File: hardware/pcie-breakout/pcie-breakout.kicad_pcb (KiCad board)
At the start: 4 copper layers, 35 x 20.3 mm, 2 parts, among them J1 Bus_PCI_Express_x1, J2 Conn_01x10

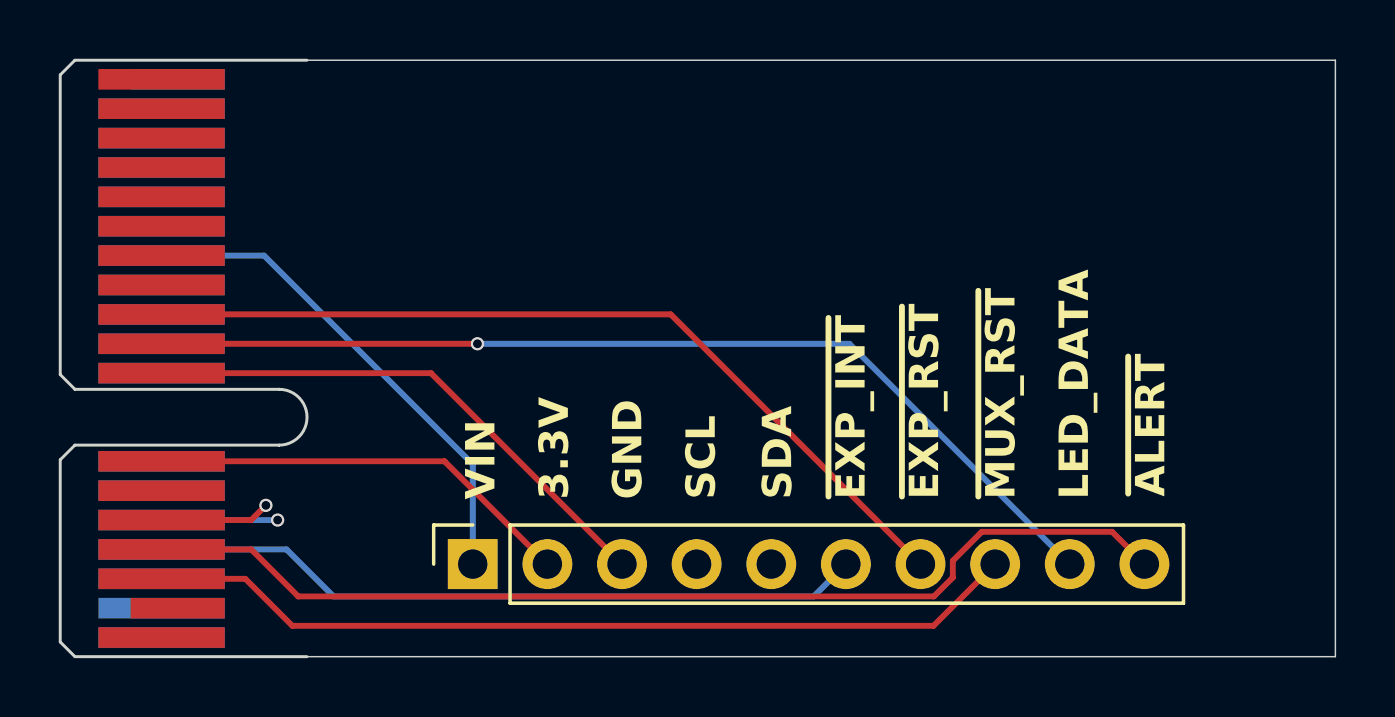
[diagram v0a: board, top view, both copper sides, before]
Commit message: chore(pcie-breakout): update 3.3v in to 5v
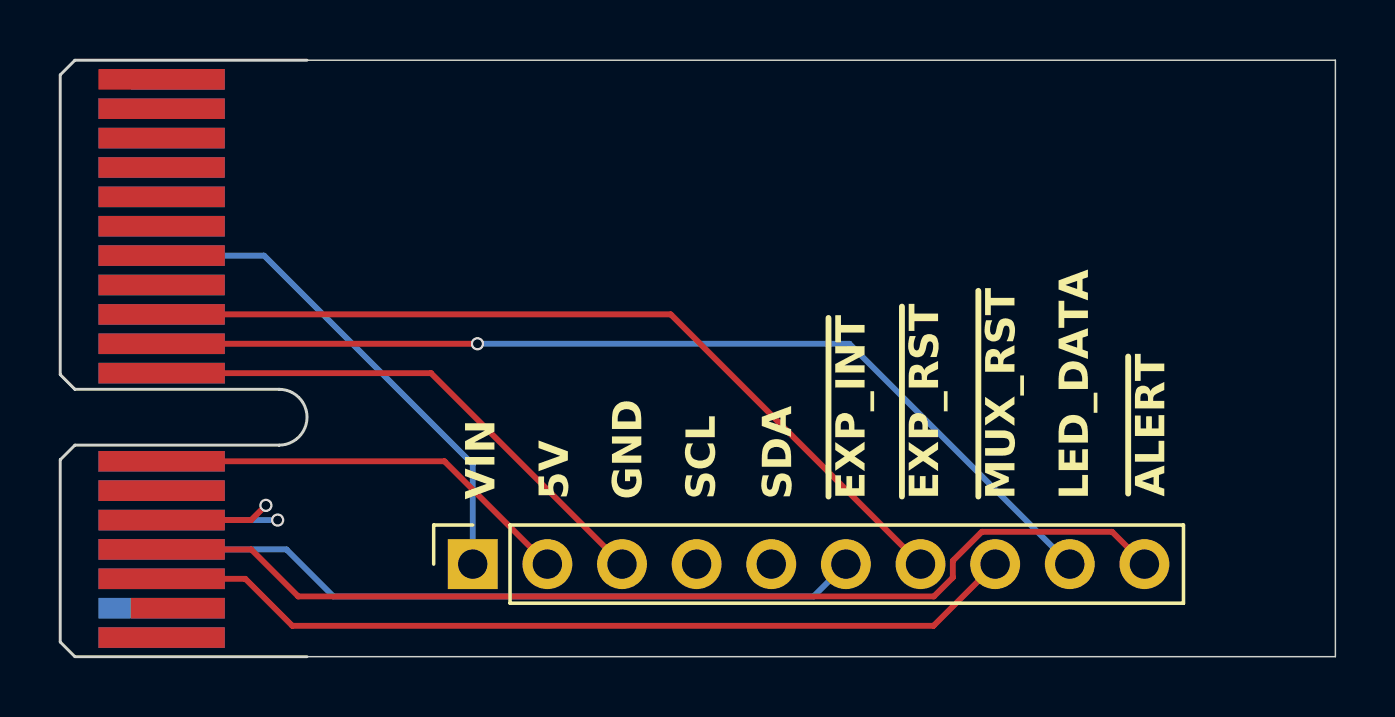
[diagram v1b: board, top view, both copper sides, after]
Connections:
- net +3.3V renamed +5V
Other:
- board text added: "5V"
- board text removed: "3.3V"
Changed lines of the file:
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@@
 		(capping no)
 		(filling no)
-		(zone_defaults)
 		(pcbplotparams
 			(layerselection 0x00000000_00000000_55555555_5755f5ff)
@@
 			)
 		)
-		(attr exclude_from_bom)
+		(attr dnp)
 		(duplicate_pad_numbers_are_jumpers no)
 		(fp_line
@@
 			(size 0.7 4.3)
 			(layers "B.Cu" "B.Mask")
-			(net "+3.3V")
-			(pinfunction "+3.3V_A12")
+			(net "+5V")
+			(pinfunction "+5V_A12")
 			(pintype "power_in")
 		)
@@
 			(size 0.7 4.3)
 			(layers "F.Cu" "F.Mask")
-			(net "+3.3V")
-			(pinfunction "+3.3V_B12")
+			(net "+5V")
+			(pinfunction "+5V_B12")
 			(pintype "passive")
 		)
@@
 			)
 		)
-		(property "Description" ""
+		(property "Description" "Generic connector, single row, 01x10, script generated (kicad-library-utils/schlib/autogen/connector/)"
 			(at 0 0 90)
 			(layer "F.Fab")
@@
 			(layers "*.Cu" "*.Mask")
 			(remove_unused_layers no)
-			(net "+3.3V")
+			(net "+5V")
 			(pinfunction "Pin_2_2")
 			(pintype "passive")
@@
 		)
 	)
-	(gr_text "3.3V"
+	(gr_text "5V"
 		(at 137.2 84.8 90)
 		(layer "F.SilkS")
@@
 	)
 	(segment
+		(start 133.84 83.6)
+		(end 133.84 87)
+		(width 0.2)
+		(layer "B.Cu")
+		(net "VIN")
+	)
+	(segment
+		(start 123.25 76.5)
+		(end 126.74 76.5)
+		(width 0.2)
+		(layer "B.Cu")
+		(net "VIN")
+	)
+	(segment
+		(start 126.74 76.5)
+		(end 133.84 83.6)
+		(width 0.2)
+		(layer "B.Cu")
+		(net "VIN")
+	)
+	(via
+		(at 127.2 85.5)
+		(size 0.45)
+		(drill 0.3)
+		(layers "F.Cu" "B.Cu")
+		(net "/SCL")
+	)
+	(segment
+		(start 123.25 85.5)
+		(end 127.2 85.5)
+		(width 0.2)
+		(layer "B.Cu")
+		(net "/SCL")
+	)
+	(segment
+		(start 139.96 85.5)
+		(end 141.46 87)
+		(width 0.2)
+		(layer "In2.Cu")
+		(net "/SCL")
+	)
+	(segment
+		(start 127.2 85.5)
+		(end 139.96 85.5)
+		(width 0.2)
+		(layer "In2.Cu")
+		(net "/SCL")
+	)
+	(segment
+		(start 129.1 88.1)
+		(end 127.5 86.5)
+		(width 0.2)
+		(layer "B.Cu")
+		(net "/~{EXP_INT}")
+	)
+	(segment
+		(start 127.5 86.5)
+		(end 123.25 86.5)
+		(width 0.2)
+		(layer "B.Cu")
+		(net "/~{EXP_INT}")
+	)
+	(segment
+		(start 145.44 88.1)
+		(end 129.1 88.1)
+		(width 0.2)
+		(layer "B.Cu")
+		(net "/~{EXP_INT}")
+	)
+	(segment
+		(start 146.54 87)
+		(end 145.44 88.1)
+		(width 0.2)
+		(layer "B.Cu")
+		(net "/~{EXP_INT}")
+	)
+	(segment
 		(start 149.08 87)
 		(end 140.58 78.5)
@@
 	)
 	(segment
-		(start 126.1 87.5)
-		(end 123.25 87.5)
-		(width 0.2)
-		(layer "F.Cu")
-		(net "/~{MUX_RST}")
-	)
-	(segment
-		(start 127.7 89.1)
-		(end 126.1 87.5)
-		(width 0.2)
-		(layer "F.Cu")
-		(net "/~{MUX_RST}")
-	)
-	(segment
-		(start 151.62 87)
-		(end 149.52 89.1)
-		(width 0.2)
-		(layer "F.Cu")
-		(net "/~{MUX_RST}")
-	)
-	(segment
-		(start 149.52 89.1)
-		(end 127.7 89.1)
-		(width 0.2)
-		(layer "F.Cu")
-		(net "/~{MUX_RST}")
+		(start 134 79.5)
+		(end 123.25 79.5)
+		(width 0.2)
+		(layer "F.Cu")
+		(net "/LED_DATA")
+	)
+	(via
+		(at 134 79.5)
+		(size 0.45)
+		(drill 0.3)
+		(layers "F.Cu" "B.Cu")
+		(net "/LED_DATA")
+	)
+	(segment
+		(start 146.66 79.5)
+		(end 134 79.5)
+		(width 0.2)
+		(layer "B.Cu")
+		(net "/LED_DATA")
+	)
+	(segment
+		(start 154.16 87)
+		(end 146.66 79.5)
+		(width 0.2)
+		(layer "B.Cu")
+		(net "/LED_DATA")
 	)
 	(segment
@@
 		(net "/SDA")
 	)
-	(via
-		(at 127.2 85.5)
-		(size 0.45)
-		(drill 0.3)
-		(layers "F.Cu" "B.Cu")
-		(net "/SCL")
-	)
-	(segment
-		(start 123.25 85.5)
-		(end 127.2 85.5)
-		(width 0.2)
-		(layer "B.Cu")
-		(net "/SCL")
-	)
-	(segment
-		(start 139.96 85.5)
-		(end 141.46 87)
-		(width 0.2)
-		(layer "In2.Cu")
-		(net "/SCL")
-	)
-	(segment
-		(start 127.2 85.5)
-		(end 139.96 85.5)
-		(width 0.2)
-		(layer "In2.Cu")
-		(net "/SCL")
-	)
-	(segment
-		(start 133.84 83.6)
-		(end 133.84 87)
-		(width 0.2)
-		(layer "B.Cu")
-		(net "VIN")
-	)
-	(segment
-		(start 123.25 76.5)
-		(end 126.74 76.5)
-		(width 0.2)
-		(layer "B.Cu")
-		(net "VIN")
-	)
-	(segment
-		(start 126.74 76.5)
-		(end 133.84 83.6)
-		(width 0.2)
-		(layer "B.Cu")
-		(net "VIN")
-	)
-	(segment
-		(start 129.1 88.1)
-		(end 127.5 86.5)
-		(width 0.2)
-		(layer "B.Cu")
-		(net "/~{EXP_INT}")
-	)
-	(segment
-		(start 127.5 86.5)
-		(end 123.25 86.5)
-		(width 0.2)
-		(layer "B.Cu")
-		(net "/~{EXP_INT}")
-	)
-	(segment
-		(start 145.44 88.1)
-		(end 129.1 88.1)
-		(width 0.2)
-		(layer "B.Cu")
-		(net "/~{EXP_INT}")
-	)
-	(segment
-		(start 146.54 87)
-		(end 145.44 88.1)
-		(width 0.2)
-		(layer "B.Cu")
-		(net "/~{EXP_INT}")
-	)
 	(segment
 		(start 126.3 86.5)
@@
 	)
 	(segment
-		(start 134 79.5)
-		(end 123.25 79.5)
-		(width 0.2)
-		(layer "F.Cu")
-		(net "/LED_DATA")
-	)
-	(via
-		(at 134 79.5)
-		(size 0.45)
-		(drill 0.3)
-		(layers "F.Cu" "B.Cu")
-		(net "/LED_DATA")
-	)
-	(segment
-		(start 146.66 79.5)
-		(end 134 79.5)
-		(width 0.2)
-		(layer "B.Cu")
-		(net "/LED_DATA")
-	)
-	(segment
-		(start 154.16 87)
-		(end 146.66 79.5)
-		(width 0.2)
-		(layer "B.Cu")
-		(net "/LED_DATA")
+		(start 126.1 87.5)
+		(end 123.25 87.5)
+		(width 0.2)
+		(layer "F.Cu")
+		(net "/~{MUX_RST}")
+	)
+	(segment
+		(start 127.7 89.1)
+		(end 126.1 87.5)
+		(width 0.2)
+		(layer "F.Cu")
+		(net "/~{MUX_RST}")
+	)
+	(segment
+		(start 151.62 87)
+		(end 149.52 89.1)
+		(width 0.2)
+		(layer "F.Cu")
+		(net "/~{MUX_RST}")
+	)
+	(segment
+		(start 149.52 89.1)
+		(end 127.7 89.1)
+		(width 0.2)
+		(layer "F.Cu")
+		(net "/~{MUX_RST}")
 	)
 	(segment
@@
 		(width 0.2)
 		(layer "F.Cu")
-		(net "+3.3V")
+		(net "+5V")
 	)
 	(segment
@@
 		(width 0.2)
 		(layer "F.Cu")
-		(net "+3.3V")
+		(net "+5V")
 	)
 	(embedded_fonts no)
